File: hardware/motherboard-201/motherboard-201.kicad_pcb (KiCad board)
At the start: 2 copper layers, 216 x 150 mm, 116 parts, among them J1 PWR_conn, J2 DB25M, J3 MSX_Slot, J4 MSX_Slot, J5 GFX_Connector_Output, J6 CONN_JOY, J7 CONN_JOY, J8 DIN8, K1 Relay, Q1 2N2222, Q2 2N2907, SW1 Push_button, U1 62256, U10 74HC04, U11 74HC32, U12 74HC32, U13 74HC32, U14 74HC08, U15 74HC139, U16 74LS07, U17 74HC74, U19 LM311, U2 62256, U20 SST39SF0, U21 74HC138, U22 74HC138, U23 74HC157, U24 AY-3-8910, U25 74HC157, U26 74HC138, U27 74HC153, U28 82C55A, U6 Z84C00, U7 74HC74, U8 74HCT245, U9 74HCU04, Y1 3.58Mhz

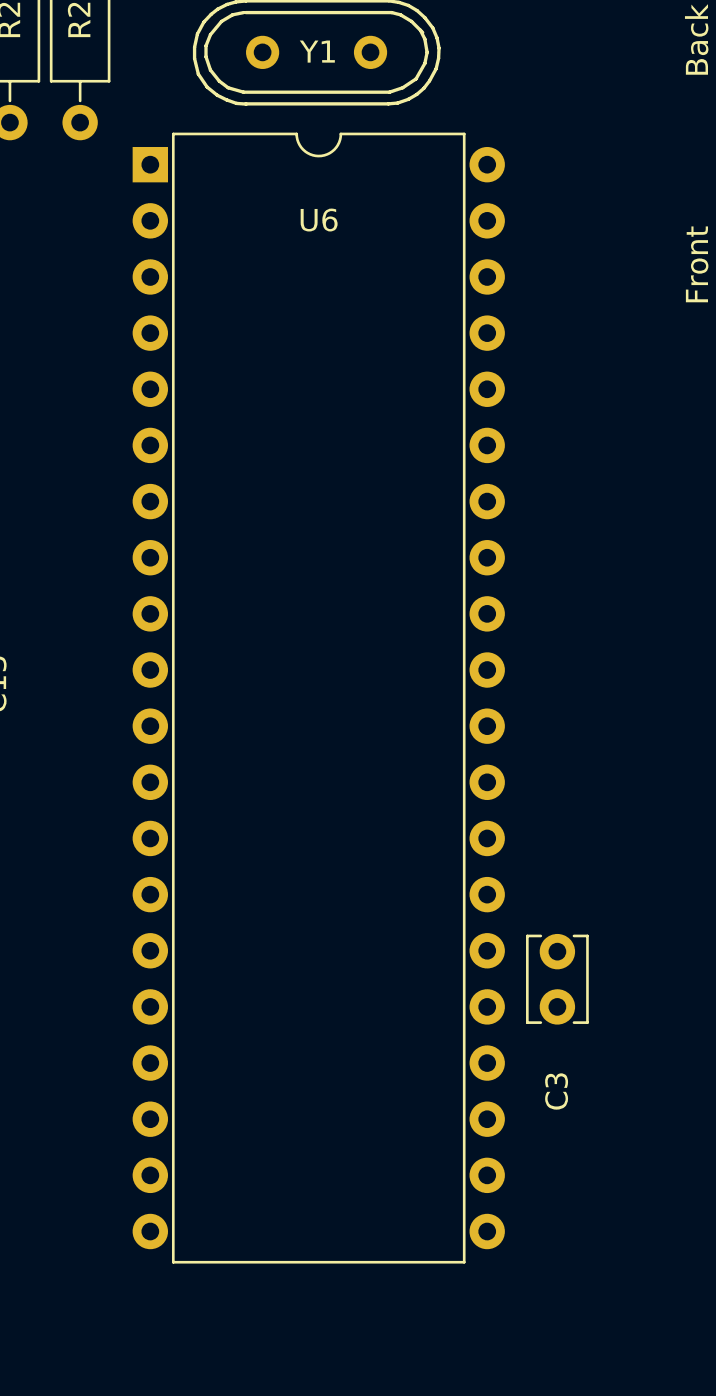
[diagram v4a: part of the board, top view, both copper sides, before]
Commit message: Use PLCC44 version of Z84 CPU
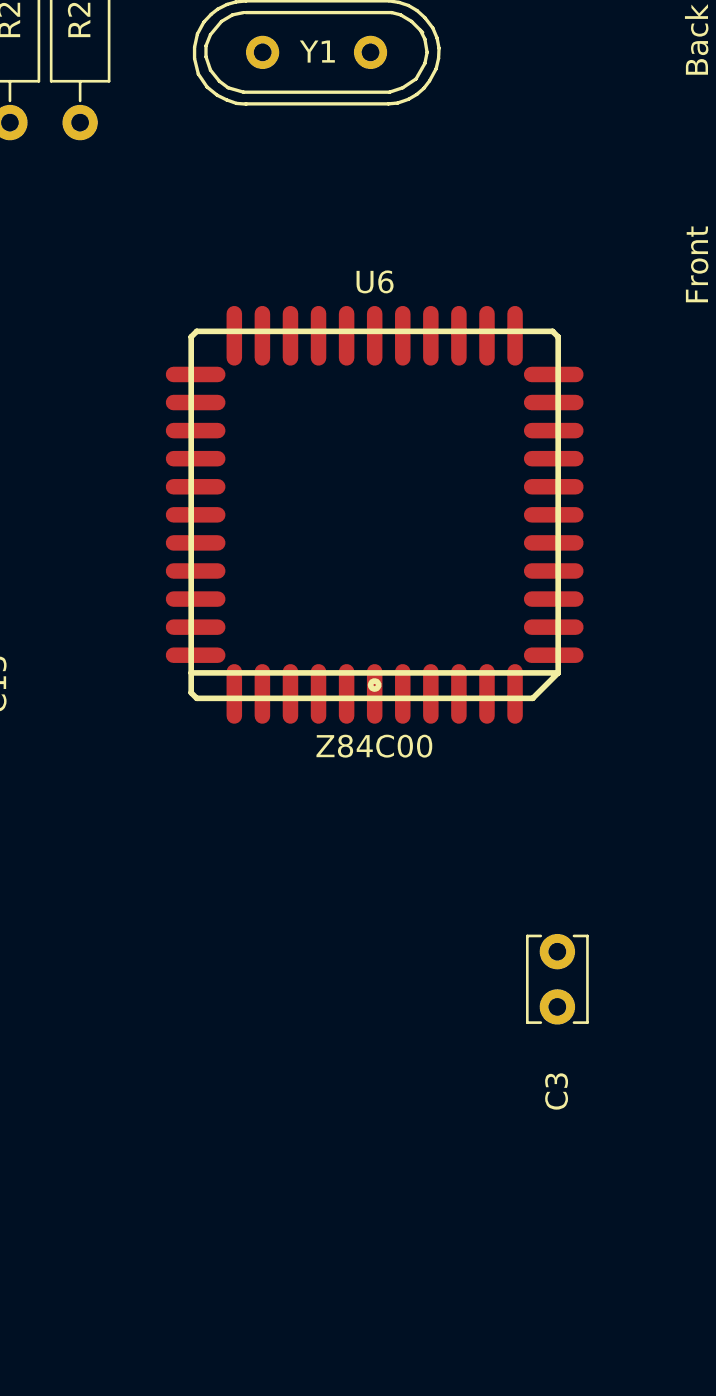
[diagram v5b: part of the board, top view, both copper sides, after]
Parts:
- U6: footprint artemisa:DIP-40_600 -> artemisa:PLCC44
- moved U6 18.8 mm to (136.9, 127.6)
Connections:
- U6 pad 10: /CPU/D6 -> /CPU/D5
- U6 pad 11: ~ -> /CPU/D6
- U6 pad 12: /CPU/D2 -> Net-(U6-Pad12)
- U6 pad 13: /CPU/D7 -> ~
- U6 pad 14: /CPU/D0 -> /CPU/D2
- U6 pad 15: /CPU/D1 -> /CPU/D7
- U6 pad 16: /~INT -> /CPU/D0
- U6 pad 17: ~ -> /CPU/D1
- U6 pad 18: Net-(U6-Pad18) -> /~INT
- U6 pad 19: /~MREQ -> ~
- U6 pad 20: /~IORQ -> Net-(U6-Pad20)
- U6 pad 21: /~RD -> /~MREQ
- U6 pad 22: /~WR -> /~IORQ
- U6 pad 23: Net-(U6-Pad23) -> /~RD
- U6 pad 25: ~ -> Net-(U6-Pad25)
- U6 pad 26: /~RESET -> /~WR
- U6 pad 27: /~M1 -> Net-(U6-Pad27)
- U6 pad 28: /~RFSH -> Net-(U6-Pad28)
- U6 pad 29: GND -> ~
- U6 pad 30: /ADDR0 -> /~RESET
- U6 pad 31: /ADDR1 -> /~M1
- U6 pad 32: /CPU/ADDR2 -> /~RFSH
- U6 pad 33: /CPU/ADDR3 -> GND
- U6 pad 34: /CPU/ADDR4 -> /ADDR0
- U6 pad 35: /CPU/ADDR5 -> /ADDR1
- U6 pad 36: /CPU/ADDR6 -> /CPU/ADDR2
- U6 pad 37: /CPU/ADDR7 -> /CPU/ADDR3
- U6 pad 38: /CPU/ADDR8 -> /CPU/ADDR4
- U6 pad 39: /CPU/ADDR9 -> /CPU/ADDR5
- U6 pad 40: /CPU/ADDR10 -> /CPU/ADDR6
- U6 pad 6: /CLK -> Net-(U6-Pad6)
- U6 pad 7: /CPU/D4 -> /CLK
- U6 pad 8: /CPU/D3 -> /CPU/D4
- U6 pad 9: /CPU/D5 -> /CPU/D3
- U7 pad 12: Net-(U6-Pad24) -> Net-(U6-Pad28)
- U7 pad 5: Net-(U6-Pad24) -> Net-(U6-Pad28)

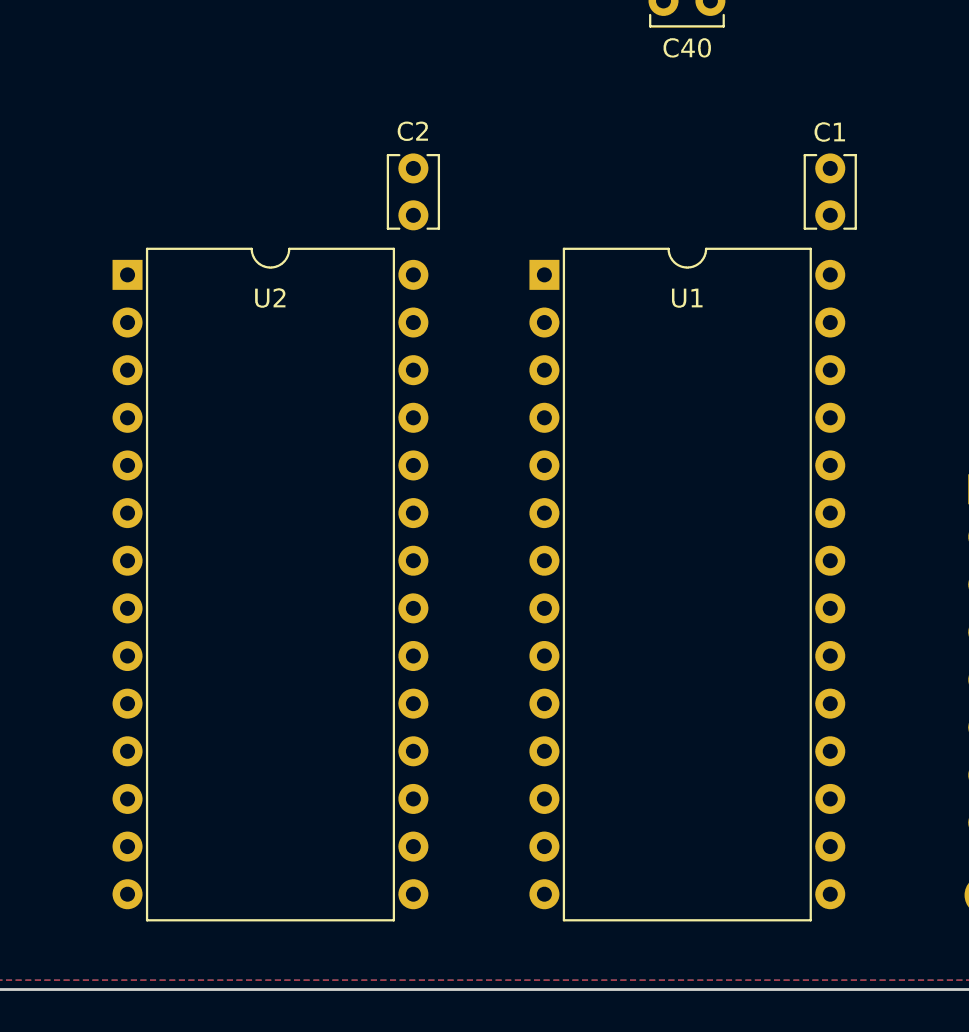
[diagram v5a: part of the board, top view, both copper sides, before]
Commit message: Use AS6C1008 as main RAM chip
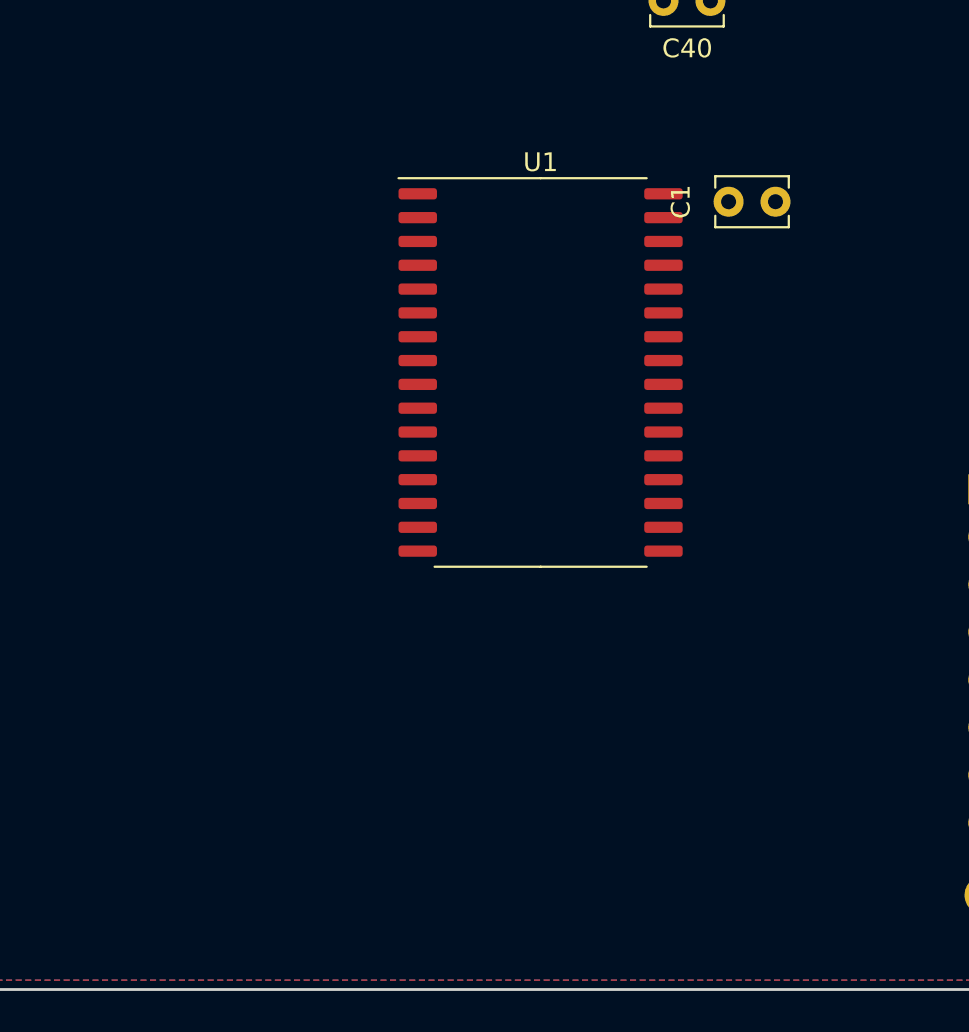
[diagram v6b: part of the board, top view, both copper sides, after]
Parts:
- removed C2: 100nF, artemisa:Disc_capacitor
- removed U2: 62256, artemisa:DIP-28_600
- U1: value 62256 -> AS6C1008; footprint artemisa:DIP-28_600 -> artemisa:SOP-32_450
- moved C1 5.47 mm to (236.9, 186.6), turned to 0 degrees
- moved U1 5.21 mm to (226.9, 195.7)
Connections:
- U1 pad 1: /ADDR14 -> Net-(U1-Pad1)
- U1 pad 10: /ADDR0 -> /CPU/ADDR2
- U1 pad 11: /CPU/DATA0 -> /ADDR1
- U1 pad 12: /CPU/DATA1 -> /ADDR0
- U1 pad 13: /CPU/DATA2 -> /CPU/DATA0
- U1 pad 14: GND -> /CPU/DATA1
- U1 pad 15: /CPU/DATA3 -> /CPU/DATA2
- U1 pad 16: /CPU/DATA4 -> GND
- U1 pad 17: /CPU/DATA5 -> /CPU/DATA3
- U1 pad 18: /CPU/DATA6 -> /CPU/DATA4
- U1 pad 19: /CPU/DATA7 -> /CPU/DATA5
- U1 pad 2: /CPU/ADDR12 -> GND
- U1 pad 20: /~RAMSL0 -> /CPU/DATA6
- U1 pad 21: /CPU/ADDR10 -> /CPU/DATA7
- U1 pad 22: /~RD -> /~SLTSL1
- U1 pad 23: /CPU/ADDR11 -> /CPU/ADDR10
- U1 pad 24: /CPU/ADDR9 -> /~RD
- U1 pad 25: /CPU/ADDR8 -> /CPU/ADDR11
- U1 pad 26: /CPU/ADDR13 -> /CPU/ADDR9
- U1 pad 27: /~WR -> /CPU/ADDR8
- U1 pad 28: ~ -> /CPU/ADDR13
- U1 pad 3: /CPU/ADDR7 -> /ADDR14
- U1 pad 4: /CPU/ADDR6 -> /CPU/ADDR12
- U1 pad 5: /CPU/ADDR5 -> /CPU/ADDR7
- U1 pad 6: /CPU/ADDR4 -> /CPU/ADDR6
- U1 pad 7: /CPU/ADDR3 -> /CPU/ADDR5
- U1 pad 8: /CPU/ADDR2 -> /CPU/ADDR4
- U1 pad 9: /ADDR1 -> /CPU/ADDR3
- U10 pad 1: /ADDR15 -> (no net)
- U10 pad 2: Net-(U10-Pad2) -> (no net)
- U11 pad 1: /~SLTSL1 -> (no net)
- U11 pad 2: /ADDR15 -> (no net)
- U11 pad 3: /~RAMSL1 -> (no net)
- U11 pad 4: /~SLTSL1 -> (no net)
- U11 pad 5: Net-(U10-Pad2) -> (no net)
- U11 pad 6: /~RAMSL0 -> (no net)
